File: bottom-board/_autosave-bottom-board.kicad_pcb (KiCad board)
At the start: 2 copper layers, 184 x 94 mm, 156 parts, among them P1 USB_B, P10 JACK_TRS_6PINS, P11 JACK_TRS_6PINS, P12 JACK_TRS_6PINS, P13 JACK_TRS_6PINS, P14 RJ45, P2 USB_A, P3 AudioJack3, P4 AS0A823-H4SB-7H, P5 BARREL_JACK, P6 AudioJack3, P7 AudioJack3, P8 HMI_DATA, P9 SERIAL_DEBUG, Q1 J110, Q12 2N7002, Q13 2N7002, Q2 J110, U1 TS2596, U10 RT9742MNGJ5, U11 6N137S, U12 ISL83491, U13 AP2120N-3.3, U2 LD1117S50TR_SOT223, U3 CODECODER-WM8731SEDS_V(SSOP28), U4 AT24CS08-STUM, U5 TS5A3159ADBVR

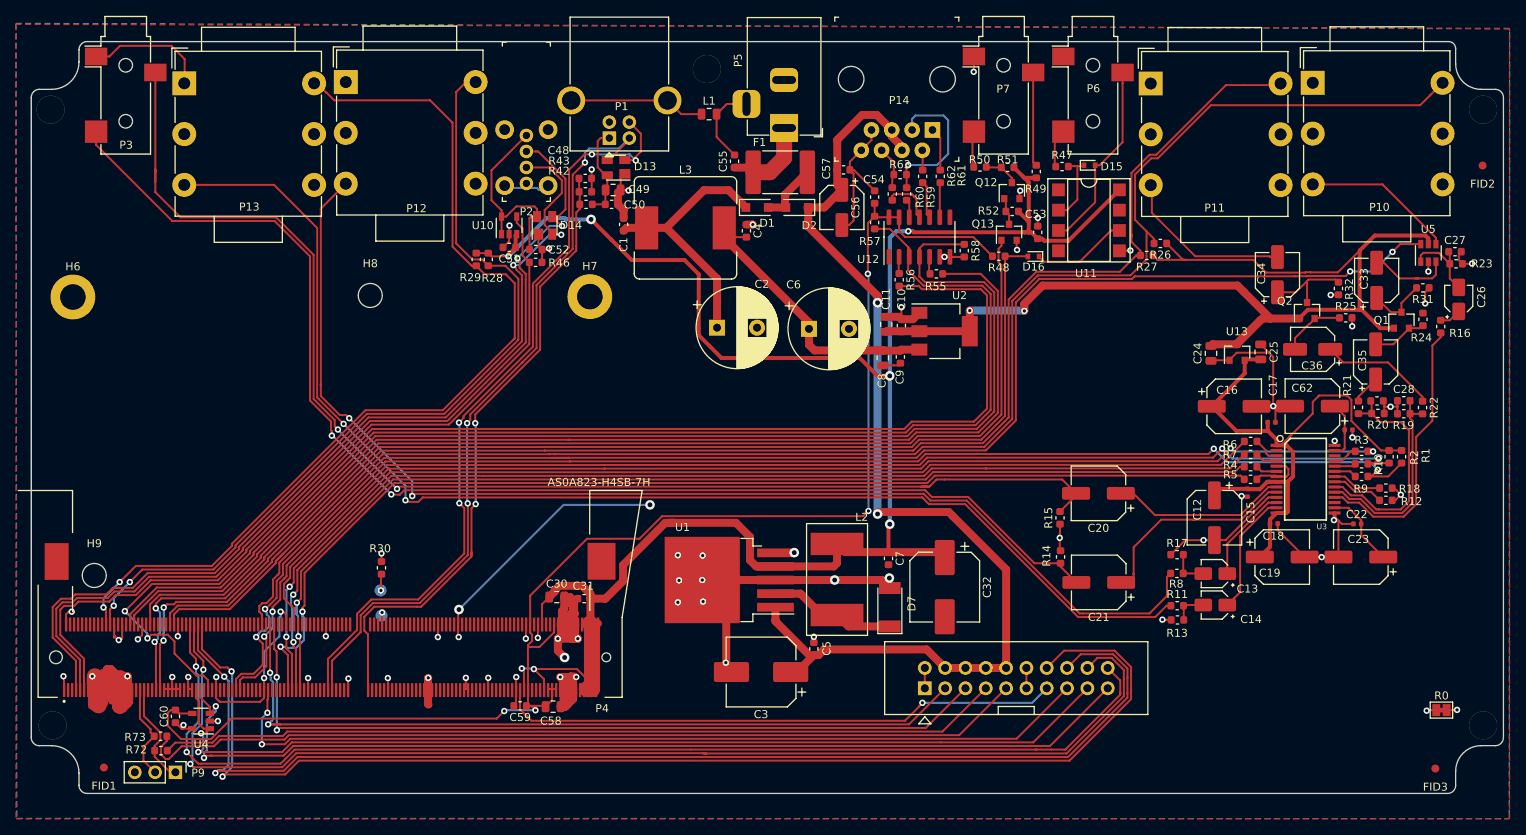
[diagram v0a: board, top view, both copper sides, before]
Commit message: change on MIDI input to TRS type A standart + cleanup
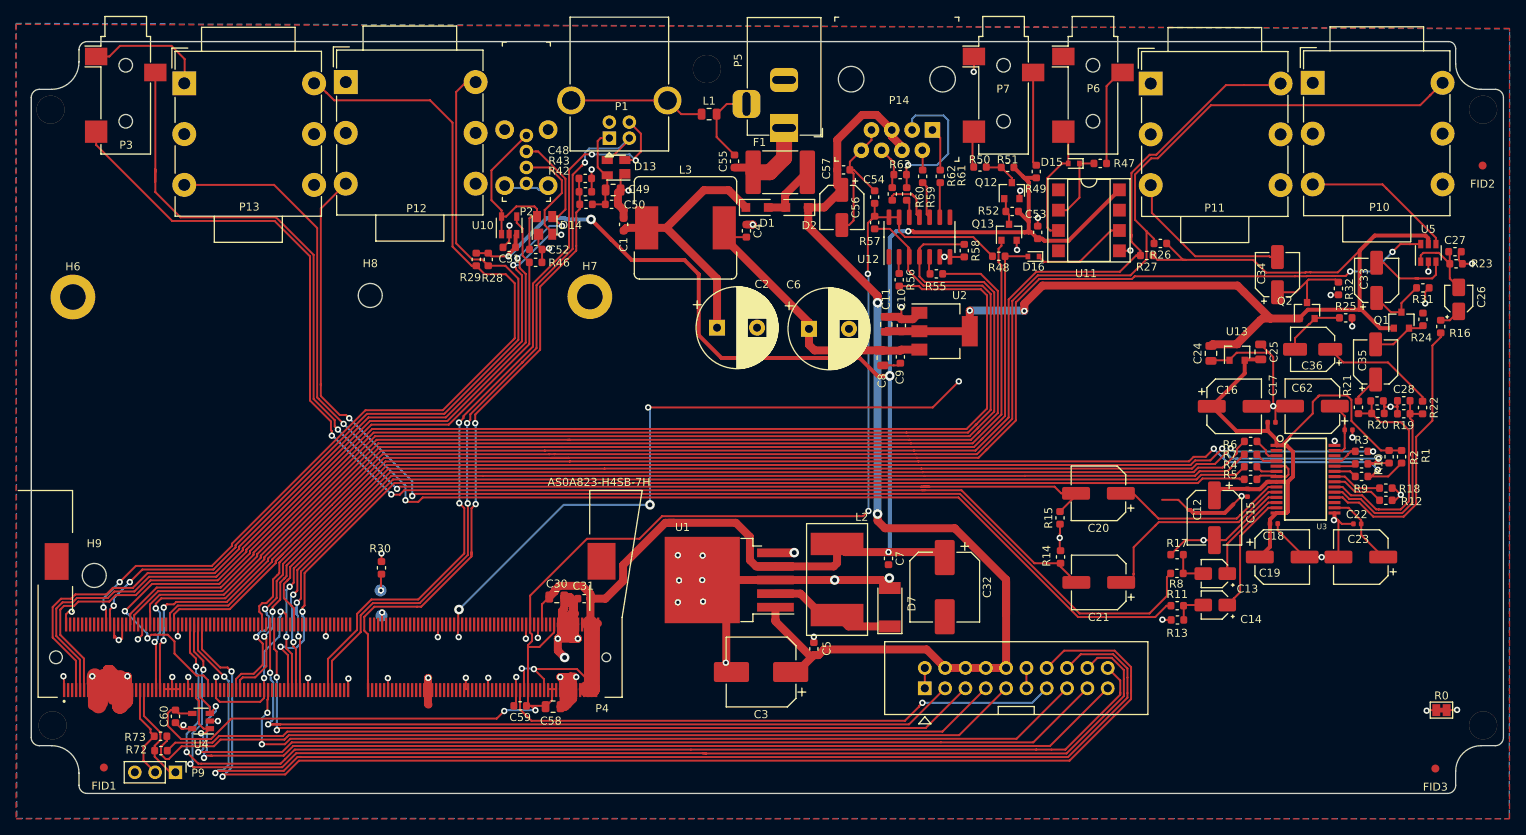
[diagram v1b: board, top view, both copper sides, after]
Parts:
- moved R47 4.79 mm to (197.0, 56.0), turned to 180 degrees
- moved D15 1.97 mm to (193.7, 56.0), turned to 180 degrees
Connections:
- P6 pad R: Net-(D15-Pad2) -> Net-(P6-PadR)
- P6 pad T: Net-(P6-PadT) -> Net-(D15-Pad2)
- R47 pad 1: Net-(P6-PadT) -> Net-(P6-PadR)
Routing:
- net GNDA: track 421.3 -> 485.2 mm, vias 75 -> 77
- net Net-(P6-PadR): track 0.00 -> 12.4 mm
- net Net-(D15-Pad2): track 24.0 -> 15.3 mm
- net Net-(P6-PadT): track 4.74 -> 0.00 mm
- net +12V: track 134.7 -> 138.3 mm
- net Net-(C20-Pad1): track 20.7 -> 21.4 mm
